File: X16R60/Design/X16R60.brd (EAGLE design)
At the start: 63.2 x 40 mm, 64 parts, among them J1 SMD Grove, K1 SMD Button Top, P1 HEXABIT__LED_MATRIX, Q1 2N7002, Q2 2N7002, SW1 LSM7-644C, U1 STM32F103C8T6, U2 XC6206P332MR, X2 8MHz

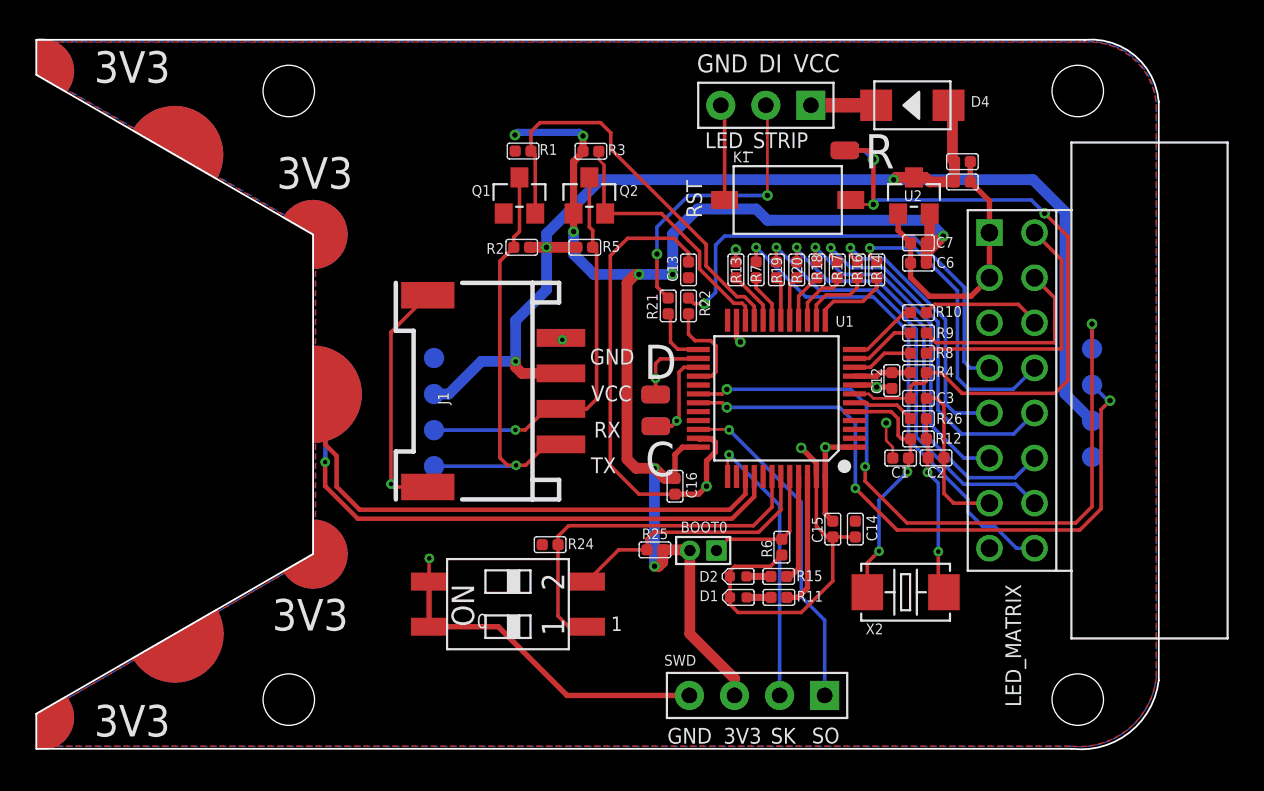
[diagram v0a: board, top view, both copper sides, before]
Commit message: - Changed MCU.. - Deleted unnecessary components.. - Regenerated output files.. - Updated BOM.. - Updated Batch_4_21 on google docs..
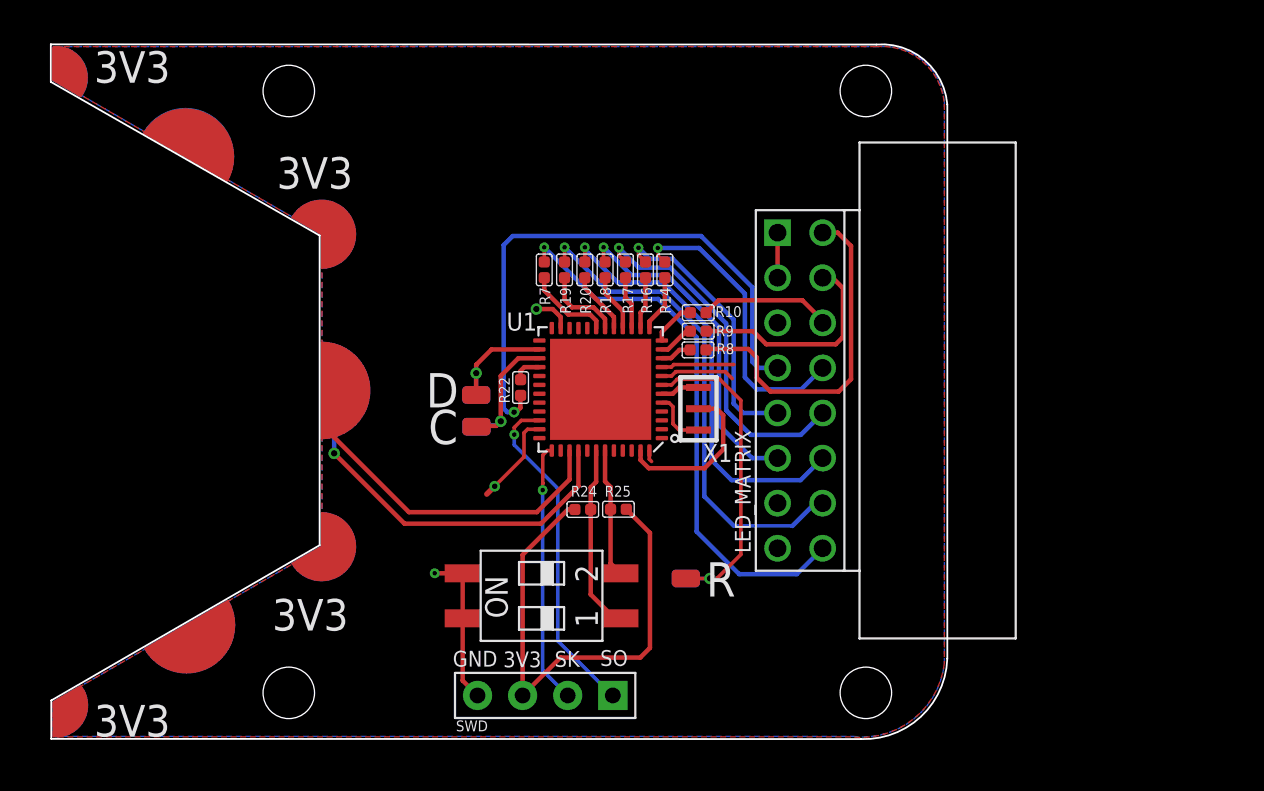
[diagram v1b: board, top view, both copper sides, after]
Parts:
- removed BOOT0: DNP, Connector-new:H2-1.5
- removed C1, C2: 22pF, Discrete-new:C0402
- removed C12, C13, C14, C15, C16, C3, C5, C7: 100nF, Discrete-new:C0402
- removed C4, C6: 10uF, Discrete-new:C0402
- removed D1, D2: LED-Blue, Discrete-new:LED-0402
- removed D4: SS14, Discrete-new:DO-214AC
- removed DB_RX, RX: RX, Discrete-new:TP-D45MIL
- removed DB_TX, TX: TX, Discrete-new:TP-D45MIL
- removed GND, GND13: GND, Discrete-new:TP-D45MIL
- removed J1: SMD Grove, Connector-new:HW4-SMD-2.0-90D
- removed K1: SMD Button Top, Discrete-new:SW2-SMD-6.0X3.0X2.5MM
- removed LED_STRIP: DNP, Connector-new:H3-2.54
- removed Q1, Q2: 2N7002, Discrete-new:SOT-23
- removed R1, R2, R3, R5: 4.7k, Discrete-new:R0402
- removed R11, R15: 680R, Discrete-new:R0402
- removed R12: 1M, Discrete-new:R0402
- removed R13, R4, R6: 10k, Discrete-new:R0402
- removed R21, R26: 33R, Discrete-new:R0402
- removed U2: XC6206P332MR, IC-new:SOT-23
- removed VCC, VCC1: VCC, Discrete-new:TP-D45MIL
- removed X2: 8MHz, Discrete-new:X2-SMD-5.0X3.2X1.3MM
- added X1: (no value), HEXABITZ_OTHER_PARTS:XTALL_CSTCE8M00G52
- P1: value HEXABIT__LED_MATRIX -> HEXABIT__P6_ONLY; device hexabitz_connectors:HEXABIT_17.32_LED_MATRIX -> hexabitz_connectors:HEXABIT_17.32_P6_ONLY
- U1: value STM32F103C8T6 -> (none); device IC-new:LQFP48 -> HEXABITZ_ICs:STM32F091CBU6
- moved R 25.7 mm to (-3.87, -10.8)
- moved R8 12.4 mm to (-3.19, 2.10)
- moved R9 12.4 mm to (-3.17, 3.15)
- moved R10 12.4 mm to (-3.17, 4.19)
- moved R20 11.9 mm to (-9.56, 6.60)
- moved R7 11.9 mm to (-11.8, 6.60)
- moved LED_MATRIX 11.9 mm to (2.57, -0.19)
- moved R14 11.9 mm to (-5.05, 6.60)
- moved R16 11.9 mm to (-6.15, 6.60)
- moved R17 11.9 mm to (-7.28, 6.60)
- moved R18 11.9 mm to (-8.42, 6.60)
- moved R19 11.9 mm to (-10.7, 6.60)
- moved SWD 11.9 mm to (-11.8, -17.4)
- moved R22 10.5 mm to (-13.2, -0.03), turned to 0 degrees
- moved C 10.1 mm to (-15.7, -2.24)
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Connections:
- removed net BOOT0: BOOT0.1, R6.2, U1.44
- removed net BOOT1: R13.2, U1.20
- removed net DB_RX: DB_RX.T, U1.31
- removed net DB_TX: DB_TX.T, U1.30
- removed net DI: LED_STRIP.2, R21.2
- removed net N$14: R22.1, U1.28
- removed net N$16: R26.2, U1.6
- removed net N$17: D4.2, LED_STRIP.1
- removed net OSC_IN: C1.2, R12.2, U1.5, X2.2
- removed net OSC_OUT: C2.2, R12.1, R26.1, X2.1
- removed net RX: J1.2, Q2.3, R5.1, RX.T
- removed net TX: J1.1, Q1.3, R2.1, TX.T
- removed net VCC: C4.2, C5.2, D4.1, J1.3, R2.2, R5.2, U2.3, VCC.T, VCC1.T
- new net EP: U1.EP
- net 3V3: now also P1.PAD_PU10, P1.PAD_PU11, P1.PAD_PU8, P1.PAD_PU9, U1.P$1, U1.P$24, U1.P$36, U1.P$48, U1.P$9; no longer BOOT0.2, C12.2, C13.2, C14.2, C15.2, C16.2, C6.2, C7.2, P1.PAD_PD11, P1.PAD_PD12, P1.PAD_PD7, P1.PAD_PD8, Q1.1, Q2.1, R1.2, R3.2, R4.1, U1.1, U1.24, U1.36, U1.48, U1.9, U2.2
- net GND: now also P1.PAD_PD10, P1.PAD_PD11, P1.PAD_PD8, P1.PAD_PD9, U1.P$23, U1.P$35, U1.P$47, U1.P$8, X1.P$2; no longer C1.1, C12.1, C13.1, C14.1, C15.1, C16.1, C2.1, C3.1, C4.1, C5.1, C6.1, C7.1, D1.-, D2.-, GND.T, GND13.T, J1.4, J1.SS1, J1.SS2, K1.1, LED_STRIP.3, P1.PAD_PU11, P1.PAD_PU12, P1.PAD_PU7, P1.PAD_PU8, R13.1, R6.1, U1.23, U1.35, U1.47, U1.8, U2.1
- net LED1: now also U1.P$45; no longer R15.2, U1.45
- net LED2: now also U1.P$46; no longer R11.2, U1.46
- net N$1: now also U1.P$5, X1.P$3; no longer D1.+, R11.1
- net N$10: now also U1.P$12; no longer U1.12
- net N$11: now also R20.1, U1.P$17; no longer R7.1, U1.19
- net N$12: now also R19.1, U1.P$18; no longer R20.1, U1.17
- net N$15: now also R22.1, U1.P$28; no longer R21.1, U1.25
- net N$18: now also D.P$1, D.P$2, U1.P$26; no longer C.P$1, C.P$2, U1.27
- net N$19: now also C.P$1, C.P$2, U1.P$27; no longer D.P$1, D.P$2, U1.26
- net N$2: now also R14.2, U1.P$13; no longer R19.1, U1.18
- net N$21: now also R7.1, U1.P$19; no longer R17.2, U1.15
- net N$3: now also U1.P$10; no longer U1.10
- net N$4: now also U1.P$6, X1.P$1; no longer D2.+, R15.1
- net N$6: now also U1.P$14; no longer U1.14
- net N$7: now also R17.2, U1.P$15; no longer R14.2, U1.13
- net N$8: now also U1.P$16; no longer U1.16
- net N$9: now also U1.P$11; no longer U1.11
- net NRST: now also U1.P$7; no longer C3.2, K1.P$2, R4.2, U1.7
- net RX_L: now also U1.P$22; no longer Q2.2, R3.1, U1.22
- net SK: now also U1.P$37; no longer U1.37
- net SO: now also U1.P$34; no longer U1.34
- net SW1: now also U1.P$42; no longer U1.42
- net SW2: now also U1.P$43; no longer U1.43
- net TX_L: now also U1.P$21; no longer Q1.2, R1.1, U1.21
- net USART5_RX: now also P1.PAD_PD3, U1.P$40; no longer P1.PAD_PU6, U1.40
- net USART5_TX: now also P1.PAD_PU3, U1.P$39; no longer P1.PAD_PD6, U1.39
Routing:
- net GND: track 120.2 -> 32.3 mm, vias 9 -> 3
- net VCC: track 70.6 -> 0.00 mm, vias 3 -> 0
- net 3V3: track 84.0 -> 33.4 mm, vias 9 -> 0
- net DB_TX: track 40.1 -> 0.00 mm, vias 3 -> 0
- net DB_RX: track 36.0 -> 0.00 mm, vias 3 -> 0
- net TX: track 25.0 -> 0.00 mm, vias 1 -> 0
- net TX_L: track 23.8 -> 0.00 mm
- net NRST: track 41.9 -> 18.8 mm, vias 3 -> 1
- net RX: track 22.5 -> 0.00 mm, vias 1 -> 0
- net DI: track 16.3 -> 0.00 mm, vias 2 -> 0
- net RX_L: track 15.1 -> 0.00 mm
- net OSC_IN: track 14.0 -> 0.00 mm, vias 2 -> 0
- net SW1: track 20.8 -> 10.5 mm
- net USART5_TX: track 30.4 -> 20.0 mm
- net OSC_OUT: track 10.2 -> 0.00 mm, vias 2 -> 0
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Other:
- board size 63.2 x 40 mm -> 50.5 x 39.1 mm
- board text removed: "0"
- board text removed: "1"
- board text removed: "DEBUG"
- board text removed: "DI"
- board text removed: "Grove"
- board text removed: "RST"
- board text removed: "RX"
- board text removed: "TX"
- board text removed: "VCC"

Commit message: Final..
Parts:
- added B: PAD1, Hexabitz:PAD1
- added C1: 10nF, Hexabitz:C-0603
- added C2: 1.00uF, Hexabitz:C-0805-POL
- added C3, C5, C6, C8, C9: 100nF, Hexabitz:C-0603
- added C4, C7: 4.7uF, Hexabitz:C-0805-POL
- added D1: VLMS1300-GS08, Hexabitz:VLMS1300-GS08
- added FB1: FB-TDK_MMZ1608Y300B, Hexabitz:FB-TDK_MMZ1608Y300B
- added R2: 10.0K, Hexabitz:R-0603
- added R3: 270.0R, Hexabitz:R-0603
- added R4: 0.0R, Hexabitz:R-0603
- R: value R -> PAD1
- moved SWD 34.7 mm to (-8.92, 17.2), turned to 90 degrees
- moved SW1 23.7 mm to (-8.06, 11.7), turned to 270 degrees
- moved R19 16.1 mm to (-12.9, -9.33), turned to 0 degrees
- moved R20 16.1 mm to (-11.7, -9.33), turned to 0 degrees
- moved R18 16.1 mm to (-10.6, -9.33), turned to 180 degrees
- moved R7 16.1 mm to (-14.1, -9.32), turned to 0 degrees
- moved R17 16.1 mm to (-9.41, -9.33), turned to 180 degrees
- moved R16 16.1 mm to (-8.24, -9.33), turned to 180 degrees
- moved R14 16.1 mm to (-7.06, -9.33), turned to 180 degrees
- moved R10 13.8 mm to (-5.88, -9.33), turned to 180 degrees
- moved R 13.4 mm to (-0.28, 2.11), flipped to the bottom
- moved R25 12.8 mm to (-11.9, 5.22), turned to 270 degrees
- moved R9 12.6 mm to (-4.74, -9.33), turned to 180 degrees
- moved R8 11.4 mm to (-3.58, -9.33), turned to 180 degrees
- moved R24 11.1 mm to (-10.2, 4.20), turned to 90 degrees
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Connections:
- removed net 3V3: P1.PAD_PU10, P1.PAD_PU11, P1.PAD_PU8, P1.PAD_PU9, R24.2, R25.2, SWD.3, U1.P$1, U1.P$24, U1.P$36, U1.P$48, U1.P$9
- removed net EP: U1.EP
- removed net NRST: R.P$1, R.P$2, U1.P$7
- new net B1: B.P$1, B.P$2, R2.2, U1.P$44
- new net N$14: D1.A, R3.1
- new net N$16: R3.2, U1.P$32
- new net R3: C8.1, R.P$1, R.P$2, U1.P$7
- new net VDD: C3.1, C4.1, C5.1, C6.1, C7.1, C9.1, FB1.2, P1.PAD_PU10, P1.PAD_PU11, P1.PAD_PU8, P1.PAD_PU9, R24.2, R25.2, SWD.3, U1.P$1, U1.P$24, U1.P$36, U1.P$48
- new net VDDA: C1.1, C2.1, FB1.1, U1.P$9
- new net VSSA: C1.2, C2.2, R4.2, U1.P$8
- net GND: now also C3.2, C4.2, C5.2, C6.2, C7.2, C8.2, C9.2, D1.C, R2.1, R4.1, U1.EP; no longer U1.P$8
- net N$1: now also X1.P$1; no longer X1.P$3
- net N$4: now also X1.P$3; no longer X1.P$1
- net SW1: now also R25.1, SW1.2; no longer R24.1, SW1.1
- net SW2: now also R24.1, SW1.1; no longer R25.1, SW1.2
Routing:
- net VDD: track 0.00 -> 34.4 mm, vias 0 -> 3
- net 3V3: track 33.4 -> 0.00 mm
- net NRST: track 18.8 -> 0.00 mm, vias 1 -> 0
- net C: track 7.46 -> 23.1 mm
- net R3: track 0.00 -> 12.1 mm, vias 0 -> 1
- net B: track 12.3 -> 23.7 mm
- net VDDA: track 0.00 -> 7.94 mm
- net GND: track 32.3 -> 24.7 mm, vias 3 -> 1
- net B1: track 0.00 -> 7.62 mm, vias 0 -> 1
- net VSSA: track 0.00 -> 7.38 mm
- net CLK: track 31.2 -> 24.3 mm, vias 1 -> 0
- net N$3: track 1.79 -> 7.88 mm, vias 0 -> 1
- net D: track 16.8 -> 22.5 mm, vias 1 -> 0
- net OE: track 32.2 -> 37.1 mm, vias 1 -> 0
- net N$9: track 2.03 -> 6.80 mm, vias 0 -> 1
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- added copper zone on layer 1, net VDD
- removed copper zone on layer 1, net 3V3
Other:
- board text added: "P1"
- board text added: "R"
